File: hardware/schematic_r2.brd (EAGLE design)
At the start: 50.8 x 38.1 mm, 41 parts, among them J1 SMA_EDGE, U1 HX1, U2 TPS62160, U3 LMC6482

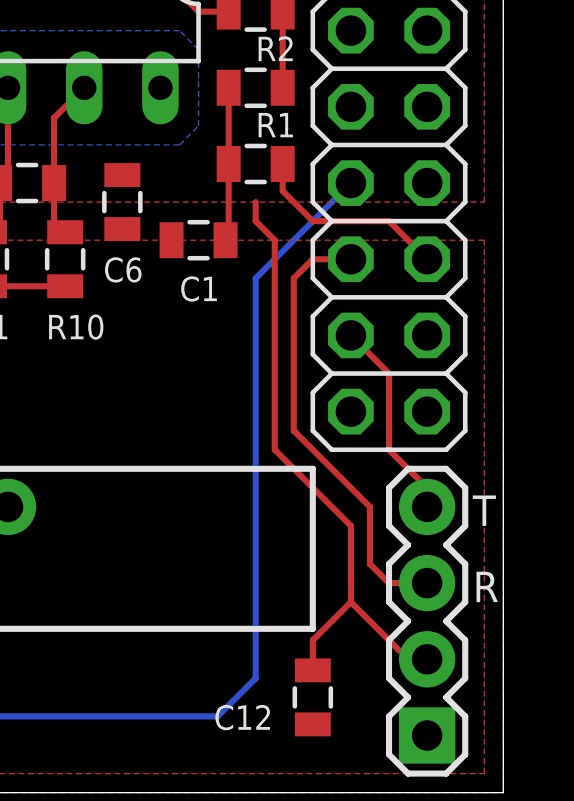
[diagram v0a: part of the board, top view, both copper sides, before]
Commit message: fixed TX RX naming for copernicus (was swapped), fixed AX.25 PWM output port to correct one
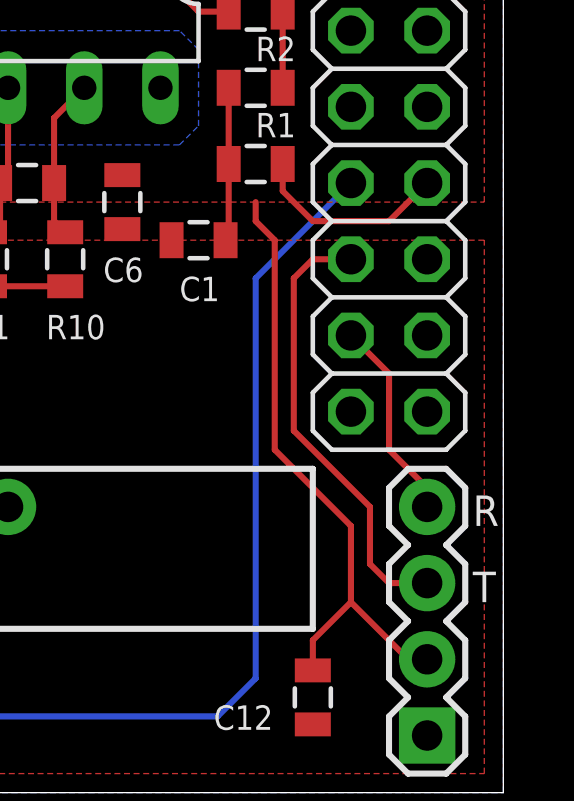
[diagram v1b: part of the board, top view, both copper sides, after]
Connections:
- net PWMOUT: now also TIVA_2.14; no longer TIVA_2.16
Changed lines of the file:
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@@
 <text x="9.906" y="27.305" size="1.016" layer="21">T</text>
 <text x="9.906" y="24.765" size="1.016" layer="21">R</text>
-<text x="49.784" y="6.35" size="1.016" layer="21">R</text>
-<text x="49.784" y="8.89" size="1.016" layer="21">T</text>
+<text x="49.784" y="6.35" size="1.016" layer="21">T</text>
+<text x="49.784" y="8.89" size="1.016" layer="21">R</text>
 </plain>
 <attributes>
@@
 <signals>
 <signal name="PWMOUT">
-<contactref element="TIVA_2" pad="16"/>
 <contactref element="R1" pad="1"/>
-<wire x1="48.26" y1="17.78" x2="46.99" y2="19.05" width="0.2032" layer="1"/>
 <wire x1="46.99" y1="19.05" x2="44.45" y2="19.05" width="0.2032" layer="1"/>
 <wire x1="44.45" y1="19.05" x2="43.445" y2="20.055" width="0.2032" layer="1"/>
 <wire x1="43.445" y1="20.955" x2="43.445" y2="20.055" width="0.2032" layer="1"/>
+<contactref element="TIVA_2" pad="14"/>
+<wire x1="46.99" y1="19.05" x2="48.26" y2="20.32" width="0.2032" layer="1"/>
 </signal>
 <signal name="PWMF1">

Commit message: Fixed #26: fix PCB bugs in Revision 2 schematics and board
Note that subsequent flights should really use an STM32-based telemetry board to get better power usage and weight.
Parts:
- removed G1: AB9V, battery:AB9V
- removed U$2: (no value), HAB:SWIFT
- added C13: 68u, SparkFun-Passives:CPOL-RADIAL-10UF-25V
- added FRAME1: FRAME-LETTERNO_PACKAGE, SparkFun-Aesthetics:DUMMY
- added JP5, JP6: SENSORS, SparkFun-Connectors:1X04
- added TP1, TP2: MCS08, solpad:MCS08
- JP1: device SparkFun-Connectors:1X03 -> SparkFun-Connectors:1X04
- moved JP1 8.03 mm to (19.7, 21.6)
- moved R5 6.54 mm to (24.1, 34.3)
- moved C4 5.75 mm to (22.2, 34.3)
- moved L1 4.26 mm to (22.7, 29.2)
- moved C9 4.26 mm to (16.6, 31.8)
- moved C10 4.26 mm to (20.3, 24.8)
- moved R12 4.26 mm to (20.3, 26.7)
- moved R13 4.26 mm to (17.1, 26.7)
- moved R14 4.26 mm to (19.7, 31.8)
- moved U2 4.26 mm to (18.4, 29.2)
- moved R6 3.24 mm to (19.7, 34.3)
- moved C3 1.27 mm to (29.2, 31.1)
- moved SJ1 1.27 mm to (17.8, 12.1)
- moved JP3 1.27 mm to (8.26, 34.3)
- moved R3 0.90 mm to (29.2, 27.9), turned to 90 degrees
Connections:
- net +3V3: now also JP5.1, JP6.1
- net +5V: now also JP1.1
- net +9V: now also C13.1, TP1.MP; no longer G1.+
- net GNDA: now also C13.2, JP1.3, JP5.2, JP6.2, TP2.MP; no longer G1.-, JP1.2
- net SCL: now also JP1.4, JP5.4, JP6.4; no longer JP1.3
- net SDA: now also JP1.2, JP5.3, JP6.3; no longer JP1.1
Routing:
- net SDA: track 12.2 -> 19.8 mm
- net SCL: track 10.1 -> 17.7 mm
- net +3V3: track 49.7 -> 56.8 mm
- net +9V: track 11.7 -> 16.3 mm, vias 0 -> 1
- net HPIN: track 12.5 -> 10.7 mm
- net VBAT: track 24.0 -> 25.6 mm
- net HPOUT: track 9.85 -> 10.7 mm
- net GNDA: track 23.9 -> 23.3 mm
- net VRX: track 6.77 -> 6.24 mm
- net VTX: track 6.77 -> 6.24 mm
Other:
- board text added: "+"
- board text added: "-"
- board text added: "HAB Project Revision B"
- board text removed: "HAB Project, Revision B"
- board text removed: "~stcarlso"
